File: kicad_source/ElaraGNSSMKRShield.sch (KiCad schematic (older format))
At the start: 26 parts, among them CN1 ARDUINO_MKR, U1 TPS736XX, U2 WIRL-POSI_Elara-I, U3 PCA9306

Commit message: updated schematic and board
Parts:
- added CN2: 60312202114509, CON_wuerth:WR-SMA-PCB, symbol CON_wuerth:60312202114509
- added R16: 0R, resistors:R_0603, symbol devices:R_0603
- added W1: TEST_1P, wire_pads:SolderWirePad_single_1mmSMD, symbol mechanical-connectors:TEST_1P
- D1: renamed from D?; footprint (none) -> LEDs:LED_0603
- gave numbers to parts that had none: 5
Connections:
- net labels added: RESET, WAKE_UP, WAKE_UP_1V8, WAKE_UP_R
- wire segments 100 -> 118
- no-connect marks 11 -> 20
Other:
- note added: "propagation delay max. 4.1 ns"
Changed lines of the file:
@@
 encoding utf-8
 Sheet 1 1
-Title ""
-Date ""
-Rev ""
-Comp ""
+Title "ElaraGNSSMKRShield"
+Date "2020-11-15"
+Rev "0.1"
+Comp "generationmake"
 Comment1 ""
 Comment2 ""
@@
 Text Label 1600 2100 0    50   ~ 0
 1PPS_1V8
-NoConn ~ 3150 2200
-NoConn ~ 3150 2400
 $Comp
 L devices:R_0603 R2
@@
 I2C_DAT
 $Comp
-L IC_logic:SN74LVC2G34 U?
+L IC_logic:SN74LVC2G34 U4
 U 1 1 5FB270EC
 P 6750 3050
-F 0 "U?" H 7000 3547 60  0000 C CNN
+F 0 "U4" H 7000 3547 60  0000 C CNN
 F 1 "SN74LVC2G34" H 7000 3441 60  0000 C CNN
 F 2 "SOT_TO:SOT-23-6" H 7050 2900 60  0001 C CNN
@@
 $EndComp
 $Comp
-L devices:C_0603 C?
+L devices:C_0603 C5
 U 1 1 5FB2A07C
 P 7450 3200
-F 0 "C?" H 7542 3246 50  0000 L CNN
+F 0 "C5" H 7542 3246 50  0000 L CNN
 F 1 "C_0603" H 7542 3155 50  0000 L CNN
 F 2 "capacitors:C_0603" H 7450 3050 50  0001 C CNN
@@
 $EndComp
 $Comp
-L power-supply:+3V3 #PWR?
+L power-supply:+3V3 #PWR023
 U 1 1 5FB2AD74
 P 7450 2700
-F 0 "#PWR?" H 7450 2550 50  0001 C CNN
+F 0 "#PWR023" H 7450 2550 50  0001 C CNN
 F 1 "+3V3" H 7465 2873 50  0000 C CNN
 F 2 "" H 7450 2700 50  0000 C CNN
@@
 $EndComp
 $Comp
-L power-supply:GND #PWR?
+L power-supply:GND #PWR024
 U 1 1 5FB2B738
 P 7450 3350
-F 0 "#PWR?" H 7450 3100 50  0001 C CNN
+F 0 "#PWR024" H 7450 3100 50  0001 C CNN
 F 1 "GND" H 7455 3177 50  0000 C CNN
 F 2 "" H 7450 3350 50  0000 C CNN
@@
 $EndComp
 $Comp
-L power-supply:GND #PWR?
+L power-supply:GND #PWR022
 U 1 1 5FB2BFD3
 P 6550 3100
-F 0 "#PWR?" H 6550 2850 50  0001 C CNN
+F 0 "#PWR022" H 6550 2850 50  0001 C CNN
 F 1 "GND" H 6555 2927 50  0000 C CNN
 F 2 "" H 6550 3100 50  0000 C CNN
@@
 	5400 2800 6650 2800
 $Comp
-L devices:R_0603 R?
+L devices:R_0603 R15
 U 1 1 5FB3608D
 P 8250 2800
-F 0 "R?" V 8054 2800 50  0000 C CNN
+F 0 "R15" V 8054 2800 50  0000 C CNN
 F 1 "0R" V 8145 2800 50  0000 C CNN
 F 2 "resistors:R_0603" H 8250 2650 50  0001 C CNN
@@
 1PPS
 $Comp
-L devices:R_0603 R?
+L devices:R_0603 R13
 U 1 1 5FB40DA9
 P 1650 1300
-F 0 "R?" H 1709 1346 50  0000 L CNN
+F 0 "R13" H 1709 1346 50  0000 L CNN
 F 1 "10k" H 1709 1255 50  0000 L CNN
 F 2 "resistors:R_0603" H 1650 1150 50  0001 C CNN
@@
 ON_OFF
 $Comp
-L devices:Led_Small D?
+L devices:Led_Small D1
 U 1 1 5FB4C116
 P 8700 2300
-F 0 "D?" H 8700 2095 50  0000 C CNN
+F 0 "D1" H 8700 2095 50  0000 C CNN
 F 1 "Led_Small" H 8700 2186 50  0000 C CNN
-F 2 "" V 8700 2300 50  0000 C CNN
+F 2 "LEDs:LED_0603" V 8700 2300 50  0001 C CNN
 F 3 "" V 8700 2300 50  0000 C CNN
 	1    8700 2300
@@
 $EndComp
 $Comp
-L devices:R_0603 R?
+L devices:R_0603 R14
 U 1 1 5FB4D7DB
 P 8250 2300
-F 0 "R?" V 8054 2300 50  0000 C CNN
+F 0 "R14" V 8054 2300 50  0000 C CNN
 F 1 "1k" V 8145 2300 50  0000 C CNN
 F 2 "resistors:R_0603" H 8250 2150 50  0001 C CNN
@@
 $EndComp
 $Comp
-L power-supply:GND #PWR?
+L power-supply:GND #PWR025
 U 1 1 5FB4DA8C
 P 8900 2350
-F 0 "#PWR?" H 8900 2100 50  0001 C CNN
+F 0 "#PWR025" H 8900 2100 50  0001 C CNN
 F 1 "GND" H 8905 2177 50  0000 C CNN
 F 2 "" H 8900 2350 50  0000 C CNN
@@
 Wire Wire Line
 	8900 2300 8900 2350
+Wire Wire Line
+	3750 2400 3150 2400
+Text Label 3200 2400 0    50   ~ 0
+WAKE_UP_1V8
+Wire Wire Line
+	5400 3000 6650 3000
+$Comp
+L devices:R_0603 R16
+U 1 1 5FB15A80
+P 8250 3000
+F 0 "R16" V 8054 3000 50  0000 C CNN
+F 1 "0R" V 8145 3000 50  0000 C CNN
+F 2 "resistors:R_0603" H 8250 2850 50  0001 C CNN
+F 3 "" H 8250 3000 50  0000 C CNN
+	1    8250 3000
+	0    1    1    0
+$EndComp
+Wire Wire Line
+	9200 3000 8350 3000
+Wire Wire Line
+	8150 3000 7350 3000
+Text Label 5800 3000 0    50   ~ 0
+WAKE_UP_1V8
+Text Label 7650 3000 0    50   ~ 0
+WAKE_UP_R
+Text Label 8600 3000 0    50   ~ 0
+WAKE_UP
+Wire Wire Line
+	7000 5500 7700 5500
+Text Label 7150 5500 0    50   ~ 0
+WAKE_UP
+Text Notes 6200 2400 0    50   ~ 0
+propagation delay max. 4.1 ns
+NoConn ~ 7700 5900
+NoConn ~ 7700 5800
+NoConn ~ 7700 5700
+NoConn ~ 7700 5400
+NoConn ~ 7700 5300
+NoConn ~ 7700 5200
+NoConn ~ 7700 5100
+NoConn ~ 7700 5000
+NoConn ~ 7700 4900
+NoConn ~ 8900 5900
+NoConn ~ 8900 6000
+$Comp
+L mechanical-connectors:TEST_1P W1
+U 1 1 5FB51AA6
+P 3800 1550
+F 0 "W1" V 3754 1738 50  0000 L CNN
+F 1 "TEST_1P" V 3845 1738 50  0000 L CNN
+F 2 "wire_pads:SolderWirePad_single_1mmSMD" H 4000 1550 50  0001 C CNN
+F 3 "" H 4000 1550 50  0000 C CNN
+	1    3800 1550
+	0    1    1    0
+$EndComp
+Wire Wire Line
+	3150 2200 3250 2200
+Wire Wire Line
+	3250 2200 3250 1550
+Wire Wire Line
+	3250 1550 3800 1550
+Text Label 3350 1550 0    50   ~ 0
+RESET
+$Comp
+L CON_wuerth:60312202114509 CN2
+U 1 1 5FB587C1
+P 9050 1450
+F 0 "CN2" H 8422 1525 60  0000 R CNN
+F 1 "60312202114509" H 8422 1419 60  0000 R CNN
+F 2 "CON_wuerth:WR-SMA-PCB" H 8422 1419 60  0001 R CNN
+F 3 "" H 9050 1450 60  0000 C CNN
+	1    9050 1450
+	-1   0    0    -1
+$EndComp
+$Comp
+L power-supply:GND #PWR026
+U 1 1 5FB5C567
+P 8750 1800
+F 0 "#PWR026" H 8750 1550 50  0001 C CNN
+F 1 "GND" H 8755 1627 50  0000 C CNN
+F 2 "" H 8750 1800 50  0000 C CNN
+F 3 "" H 8750 1800 50  0000 C CNN
+	1    8750 1800
+	1    0    0    -1
+$EndComp
+Wire Wire Line
+	8850 1200 8750 1200
+Wire Wire Line
+	8750 1200 8750 1300
+Wire Wire Line
+	8850 1700 8750 1700
+Connection ~ 8750 1700
+Wire Wire Line
+	8750 1700 8750 1800
+Wire Wire Line
+	8850 1600 8750 1600
+Connection ~ 8750 1600
+Wire Wire Line
+	8750 1600 8750 1700
+Wire Wire Line
+	8850 1300 8750 1300
+Connection ~ 8750 1300
+Wire Wire Line
+	8750 1300 8750 1600
+Wire Wire Line
+	8850 1450 8050 1450
+Wire Wire Line
+	8050 1450 8050 2300
+Connection ~ 8050 2300
 $EndSCHEMATC

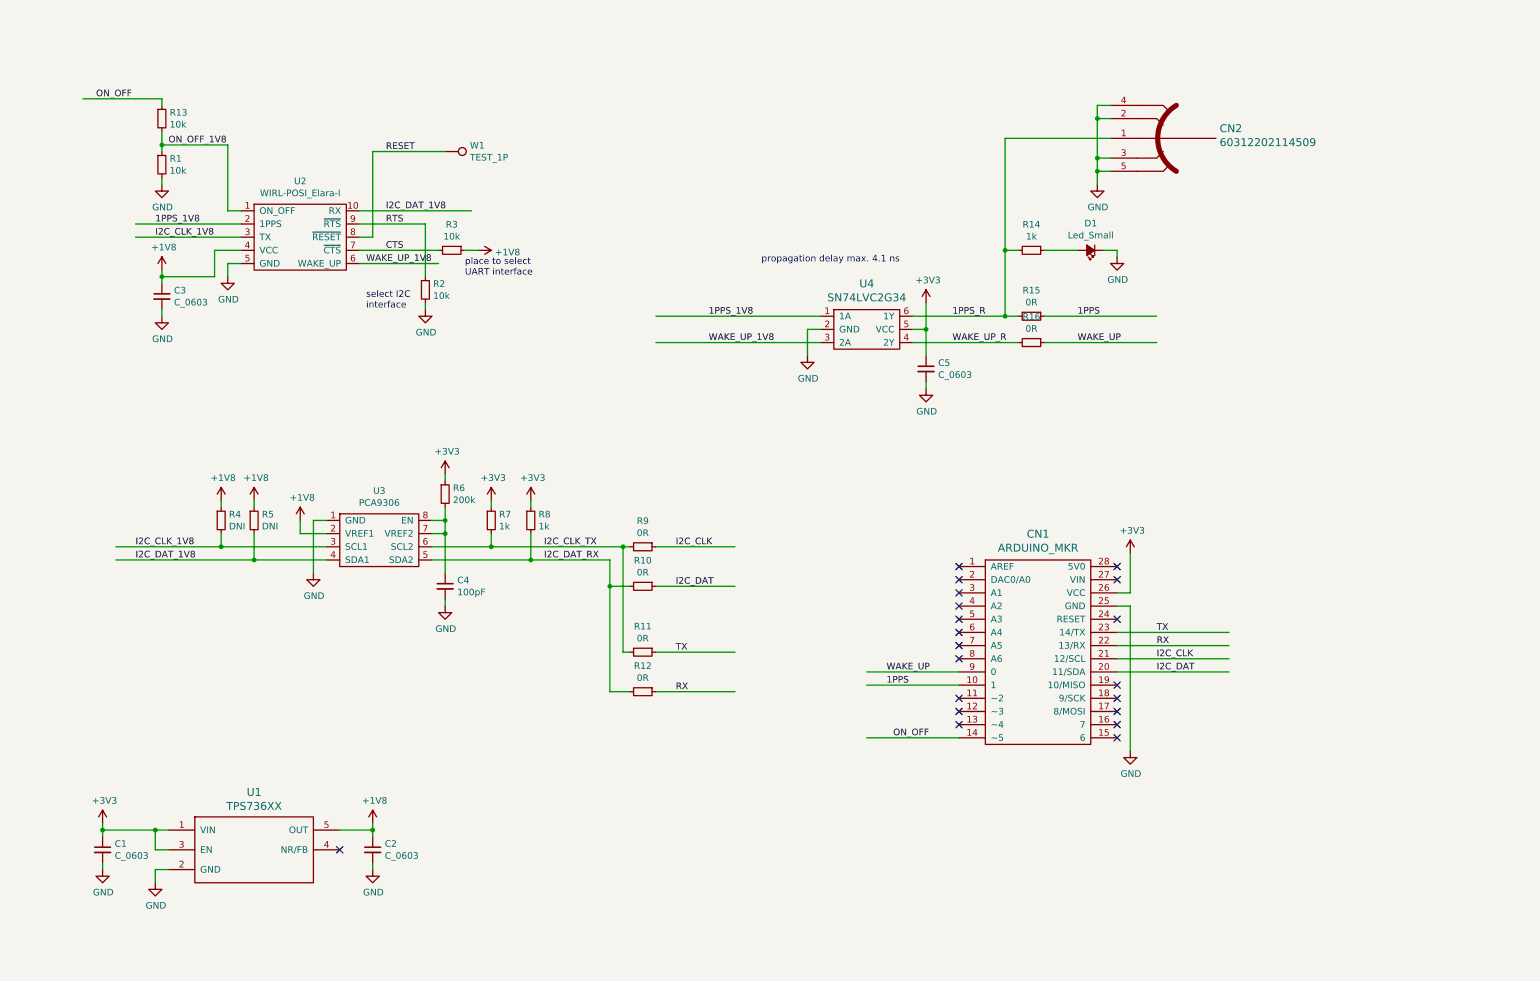
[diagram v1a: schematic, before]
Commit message: updated level shifter circuit
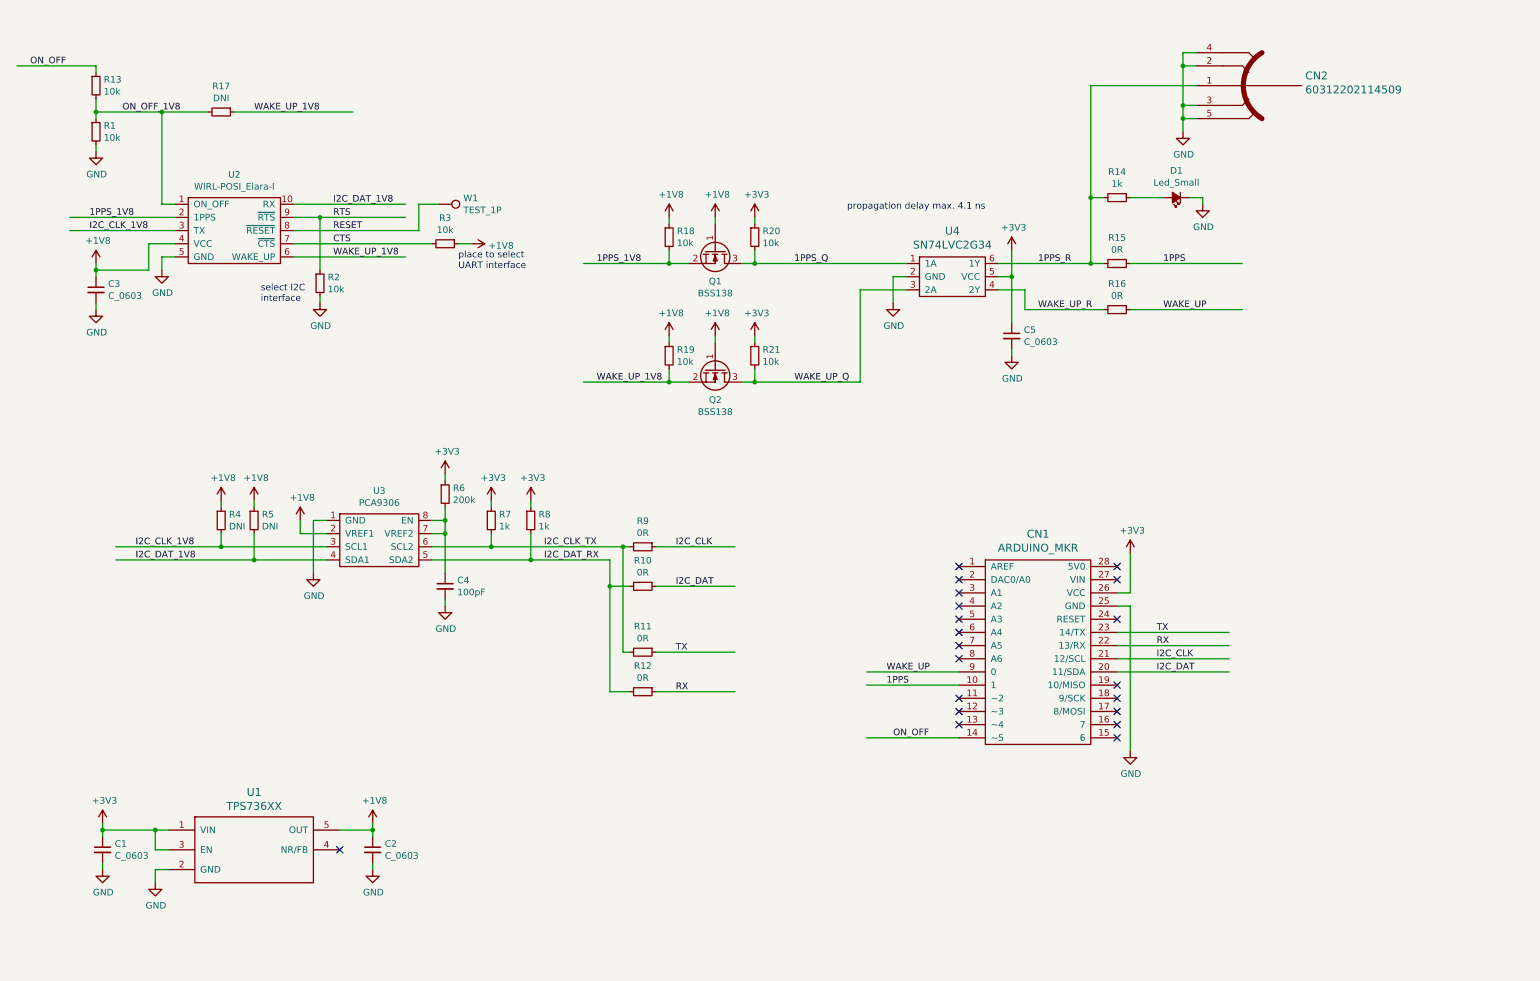
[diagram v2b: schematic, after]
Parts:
- added Q1, Q2: BSS138, SOT_TO:SOT-23, symbol devices:Q_NMOS_GSD
- added R17: DNI, resistors:R_0603, symbol devices:R_0603
- added R18, R19, R20, R21: 10k, resistors:R_0603, symbol devices:R_0603
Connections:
- net labels added: 1PPS_Q, WAKE_UP_Q
- wire segments 118 -> 141
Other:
- moved on the sheet: C3, C5, CN2, D1, R1, R13, R14, R15, R16, R2, R3, U2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

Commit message: beautified layout, added images, updated files
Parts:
- added L1: Label, labels:generationmake_small_solder, symbol devices:Label
- CN1: footprint MODULE_compute:ARDUINO_MKR_HOLES -> MODULE_compute:ARDUINO_MKR_HOLES_PINHEADER
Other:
- moved on the sheet: C1, C2, U1
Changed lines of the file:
@@
 Sheet 1 1
 Title "ElaraGNSSMKRShield"
-Date "2020-11-15"
+Date "2020-11-16"
 Rev "0.1"
 Comp "generationmake"
@@
 L voltage-regulators:TPS736XX U1
 U 1 1 5F8A34DE
-P 2350 6800
-F 0 "U1" H 2350 7187 60  0000 C CNN
-F 1 "TPS736XX" H 2350 7081 60  0000 C CNN
-F 2 "SOT_TO:SOT-23-5" H 2350 6950 60  0001 C CNN
-F 3 "" H 2350 6800 60  0000 C CNN
-	1    2350 6800
+P 2250 6200
+F 0 "U1" H 2250 6587 60  0000 C CNN
+F 1 "TPS736XX" H 2250 6481 60  0000 C CNN
+F 2 "SOT_TO:SOT-23-5" H 2250 6350 60  0001 C CNN
+F 3 "" H 2250 6200 60  0000 C CNN
+	1    2250 6200
 	1    0    0    -1
 $EndComp
@@
 L power-supply:GND #PWR03
 U 1 1 5F8A38E0
-P 1600 7100
-F 0 "#PWR03" H 1600 6850 50  0001 C CNN
-F 1 "GND" H 1605 6927 50  0000 C CNN
-F 2 "" H 1600 7100 50  0000 C CNN
-F 3 "" H 1600 7100 50  0000 C CNN
-	1    1600 7100
+P 1500 6500
+F 0 "#PWR03" H 1500 6250 50  0001 C CNN
+F 1 "GND" H 1505 6327 50  0000 C CNN
+F 2 "" H 1500 6500 50  0000 C CNN
+F 3 "" H 1500 6500 50  0000 C CNN
+	1    1500 6500
 	1    0    0    -1
 $EndComp
@@
 L power-supply:+3V3 #PWR01
 U 1 1 5F8A3C41
-P 1200 6650
-F 0 "#PWR01" H 1200 6500 50  0001 C CNN
-F 1 "+3V3" H 1215 6823 50  0000 C CNN
-F 2 "" H 1200 6650 50  0000 C CNN
-F 3 "" H 1200 6650 50  0000 C CNN
-	1    1200 6650
+P 1100 6050
+F 0 "#PWR01" H 1100 5900 50  0001 C CNN
+F 1 "+3V3" H 1115 6223 50  0000 C CNN
+F 2 "" H 1100 6050 50  0000 C CNN
+F 3 "" H 1100 6050 50  0000 C CNN
+	1    1100 6050
 	1    0    0    -1
 $EndComp
@@
 L power-supply:+1V8 #PWR04
 U 1 1 5F8A3F64
-P 3250 6650
-F 0 "#PWR04" H 3250 6500 50  0001 C CNN
-F 1 "+1V8" H 3265 6823 50  0000 C CNN
-F 2 "" H 3250 6650 50  0000 C CNN
-F 3 "" H 3250 6650 50  0000 C CNN
-	1    3250 6650
+P 3150 6050
+F 0 "#PWR04" H 3150 5900 50  0001 C CNN
+F 1 "+1V8" H 3165 6223 50  0000 C CNN
+F 2 "" H 3150 6050 50  0000 C CNN
+F 3 "" H 3150 6050 50  0000 C CNN
+	1    3150 6050
 	1    0    0    -1
 $EndComp
@@
 F 0 "CN1" H 8300 6247 60  0000 C CNN
 F 1 "ARDUINO_MKR" H 8300 6141 60  0000 C CNN
-F 2 "MODULE_compute:ARDUINO_MKR_HOLES" H 8200 6000 60  0001 C CNN
+F 2 "MODULE_compute:ARDUINO_MKR_HOLES_PINHEADER" H 8200 6000 60  0001 C CNN
 F 3 "" H 8300 5050 60  0000 C CNN
 	1    8300 5350
@@
 L devices:C_0603 C1
 U 1 1 5F8A5117
-P 1200 6850
-F 0 "C1" H 1292 6896 50  0000 L CNN
-F 1 "C_0603" H 1292 6805 50  0000 L CNN
-F 2 "capacitors:C_0603" H 1200 6700 50  0001 C CNN
-F 3 "" H 1200 6850 50  0000 C CNN
-	1    1200 6850
+P 1100 6250
+F 0 "C1" H 1192 6296 50  0000 L CNN
+F 1 "C_0603" H 1192 6205 50  0000 L CNN
+F 2 "capacitors:C_0603" H 1100 6100 50  0001 C CNN
+F 3 "" H 1100 6250 50  0000 C CNN
+	1    1100 6250
 	1    0    0    -1
 $EndComp
@@
 L power-supply:GND #PWR02
 U 1 1 5F8A62A0
-P 1200 7000
-F 0 "#PWR02" H 1200 6750 50  0001 C CNN
-F 1 "GND" H 1205 6827 50  0000 C CNN
-F 2 "" H 1200 7000 50  0000 C CNN
-F 3 "" H 1200 7000 50  0000 C CNN
-	1    1200 7000
+P 1100 6400
+F 0 "#PWR02" H 1100 6150 50  0001 C CNN
+F 1 "GND" H 1105 6227 50  0000 C CNN
+F 2 "" H 1100 6400 50  0000 C CNN
+F 3 "" H 1100 6400 50  0000 C CNN
+	1    1100 6400
 	1    0    0    -1
 $EndComp
@@
 L devices:C_0603 C2
 U 1 1 5F8A6BA6
-P 3250 6850
-F 0 "C2" H 3342 6896 50  0000 L CNN
-F 1 "C_0603" H 3342 6805 50  0000 L CNN
-F 2 "capacitors:C_0603" H 3250 6700 50  0001 C CNN
-F 3 "" H 3250 6850 50  0000 C CNN
-	1    3250 6850
+P 3150 6250
+F 0 "C2" H 3242 6296 50  0000 L CNN
+F 1 "C_0603" H 3242 6205 50  0000 L CNN
+F 2 "capacitors:C_0603" H 3150 6100 50  0001 C CNN
+F 3 "" H 3150 6250 50  0000 C CNN
+	1    3150 6250
 	1    0    0    -1
 $EndComp
@@
 L power-supply:GND #PWR05
 U 1 1 5F8A6E80
-P 3250 7000
-F 0 "#PWR05" H 3250 6750 50  0001 C CNN
-F 1 "GND" H 3255 6827 50  0000 C CNN
-F 2 "" H 3250 7000 50  0000 C CNN
-F 3 "" H 3250 7000 50  0000 C CNN
-	1    3250 7000
-	1    0    0    -1
-$EndComp
-NoConn ~ 3000 6850
-Wire Wire Line
-	3250 6750 3250 6700
-Wire Wire Line
-	3250 6950 3250 7000
-Wire Wire Line
-	3000 6700 3250 6700
-Connection ~ 3250 6700
-Wire Wire Line
-	3250 6700 3250 6650
-Wire Wire Line
-	1200 6650 1200 6700
-Wire Wire Line
-	1200 6950 1200 7000
-Wire Wire Line
-	1700 7000 1600 7000
-Wire Wire Line
-	1600 7000 1600 7100
-Wire Wire Line
-	1700 6700 1600 6700
-Connection ~ 1200 6700
-Wire Wire Line
-	1200 6700 1200 6750
-Wire Wire Line
-	1700 6850 1600 6850
-Wire Wire Line
-	1600 6850 1600 6700
-Connection ~ 1600 6700
-Wire Wire Line
-	1600 6700 1200 6700
+P 3150 6400
+F 0 "#PWR05" H 3150 6150 50  0001 C CNN
+F 1 "GND" H 3155 6227 50  0000 C CNN
+F 2 "" H 3150 6400 50  0000 C CNN
+F 3 "" H 3150 6400 50  0000 C CNN
+	1    3150 6400
+	1    0    0    -1
+$EndComp
+NoConn ~ 2900 6250
+Wire Wire Line
+	3150 6150 3150 6100
+Wire Wire Line
+	3150 6350 3150 6400
+Wire Wire Line
+	2900 6100 3150 6100
+Connection ~ 3150 6100
+Wire Wire Line
+	3150 6100 3150 6050
+Wire Wire Line
+	1100 6050 1100 6100
+Wire Wire Line
+	1100 6350 1100 6400
+Wire Wire Line
+	1600 6400 1500 6400
+Wire Wire Line
+	1500 6400 1500 6500
+Wire Wire Line
+	1600 6100 1500 6100
+Connection ~ 1100 6100
+Wire Wire Line
+	1100 6100 1100 6150
+Wire Wire Line
+	1600 6250 1500 6250
+Wire Wire Line
+	1500 6250 1500 6100
+Connection ~ 1500 6100
+Wire Wire Line
+	1500 6100 1100 6100
 $Comp
 L power-supply:+1V8 #PWR07
@@
 Wire Wire Line
 	2650 2150 3600 2150
+$Comp
+L devices:Label L1
+U 1 1 5FB4032F
+P 700 7600
+F 0 "L1" H 928 7706 60  0000 L CNN
+F 1 "Label" H 928 7600 60  0000 L CNN
+F 2 "labels:generationmake_small_solder" H 928 7494 60  0000 L CNN
+F 3 "" H 700 7600 60  0000 C CNN
+	1    700  7600
+	1    0    0    -1
+$EndComp
 $EndSCHEMATC
